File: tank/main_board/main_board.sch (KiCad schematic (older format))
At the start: 40 parts, among them J1 PowerIn, J10 Sonar2, J11 Programming Header, J12 SigOut, J13 Conn_01x01, J14 Conn_01x01, J15 Conn_01x01, J16 PowerOut, J2 Conn_01x01, J3 Conn_01x01, J4 LED, J5 Conn_01x01, J6 Spk, J7 Hall2, J8 Hall1, J9 Sonar1, Q1 2N3904, U1 LM317_TO3, U2 ATMEGA328P-PU, U3 SN754410, U4 SN754410, Y1 Crystal

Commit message: Main Board v0.2
Adjustments to main board:
- resistors were inline when they shoulda been pull-ups
- adjust crystal footprint
- IR TX needs to be on pin 3
- silkscreen should have component names
- width of motor traces increased and added ground-fill
- motor vin isn't actually connected
- motor screw terminal footprints
- fix reset line - 1 uF cap
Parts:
- removed C7: C7, Capacitors_THT:C_Disc_D4.7mm_W2.5mm_P5.00mm, symbol C_Small
- removed J1: PowerIn, JST:JST_EH_B02B-EH-A_02x2.50mm_Straight, symbol Conn_01x02
- removed J13, J14, J15, J2, J3, J5: Conn_01x01, Connectors:1pin, symbol Conn_01x01
- removed J4: LED, JST:JST_EH_B04B-EH-A_04x2.50mm_Straight, symbol Conn_01x04
- removed R5: R5, Resistors_THT:R_Axial_DIN0207_L6.3mm_D2.5mm_P7.62mm_Horizontal, symbol R
- removed R8: R8, Resistors_THT:R_Axial_DIN0207_L6.3mm_D2.5mm_P7.62mm_Horizontal, symbol R
- removed R9: R, Resistors_THT:R_Axial_DIN0207_L6.3mm_D2.5mm_P7.62mm_Horizontal, symbol R
- added C7: CP, Capacitors_THT:CP_Radial_D4.0mm_P2.00mm, symbol CP
- added J1: Conn_01x02_Male, JST:JST_EH_B02B-EH-A_02x2.50mm_Straight, symbol Conn_01x02_Male
- added J2, J3, J5: Conn_01x02, Connectors_Terminal_Blocks:TerminalBlock_4UCON_19963_02x3.5mm_Straight, symbol Conn_01x02
- added J4: Conn_01x03_Male, JST:JST_EH_B03B-EH-A_03x2.50mm_Straight, symbol Conn_01x03_Male
- J11: footprint Connectors:Wafer_Vertical17.5x5.8x7RM2.5-6 -> Pin_Headers:Pin_Header_Straight_1x06_Pitch2.54mm
- Y1: footprint Crystals:Crystal_HC52-6mm_Vertical -> Crystals:Crystal_HC49-U_Vertical
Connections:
- net labels added: IRRx, IRTx, LED0, MEnable, SCL, SPK
- net labels removed: LED2, LED3, Reset, SLC, Sonar1, Sonar2, Speaker, TurretCal, TurretEnc
- wire segments 97 -> 77
- no-connect marks 6 -> 7
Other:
- moved on the sheet: C5, C6, J10, J11, J12, J16, J6, J7, J8, J9, R10, R3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

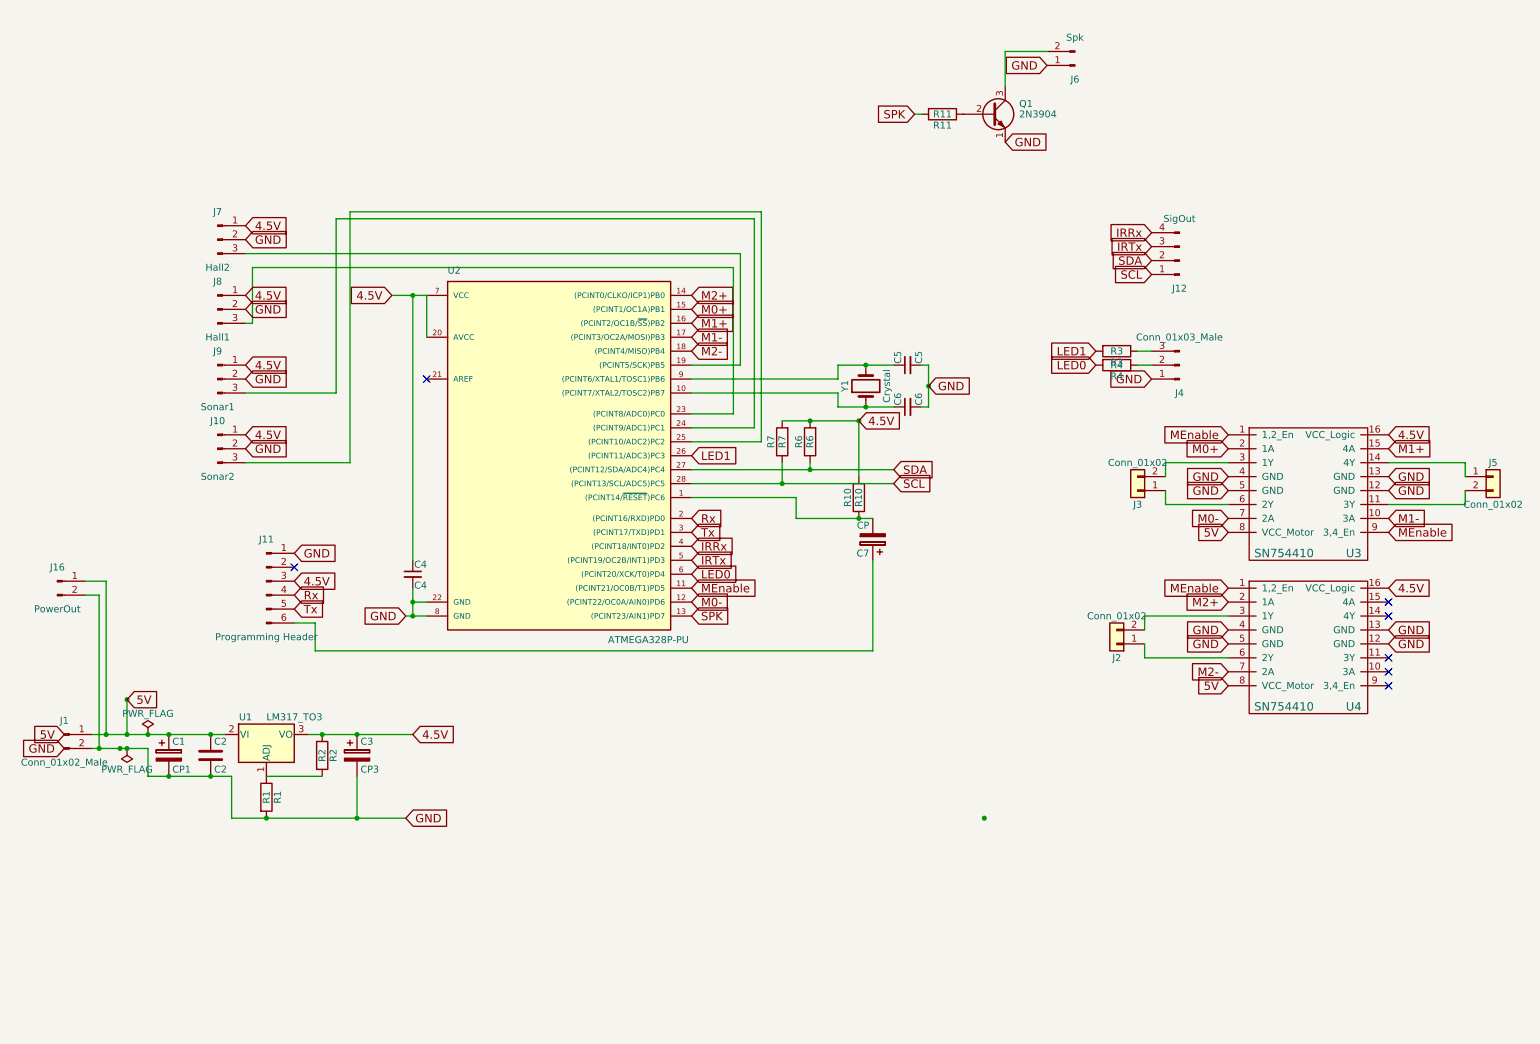
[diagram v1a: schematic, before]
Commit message: Main Board v0.3 - changed motor controllers to TB6612FNG - changed speaker transistor wiring - supports 4 LEDs, using switched ground
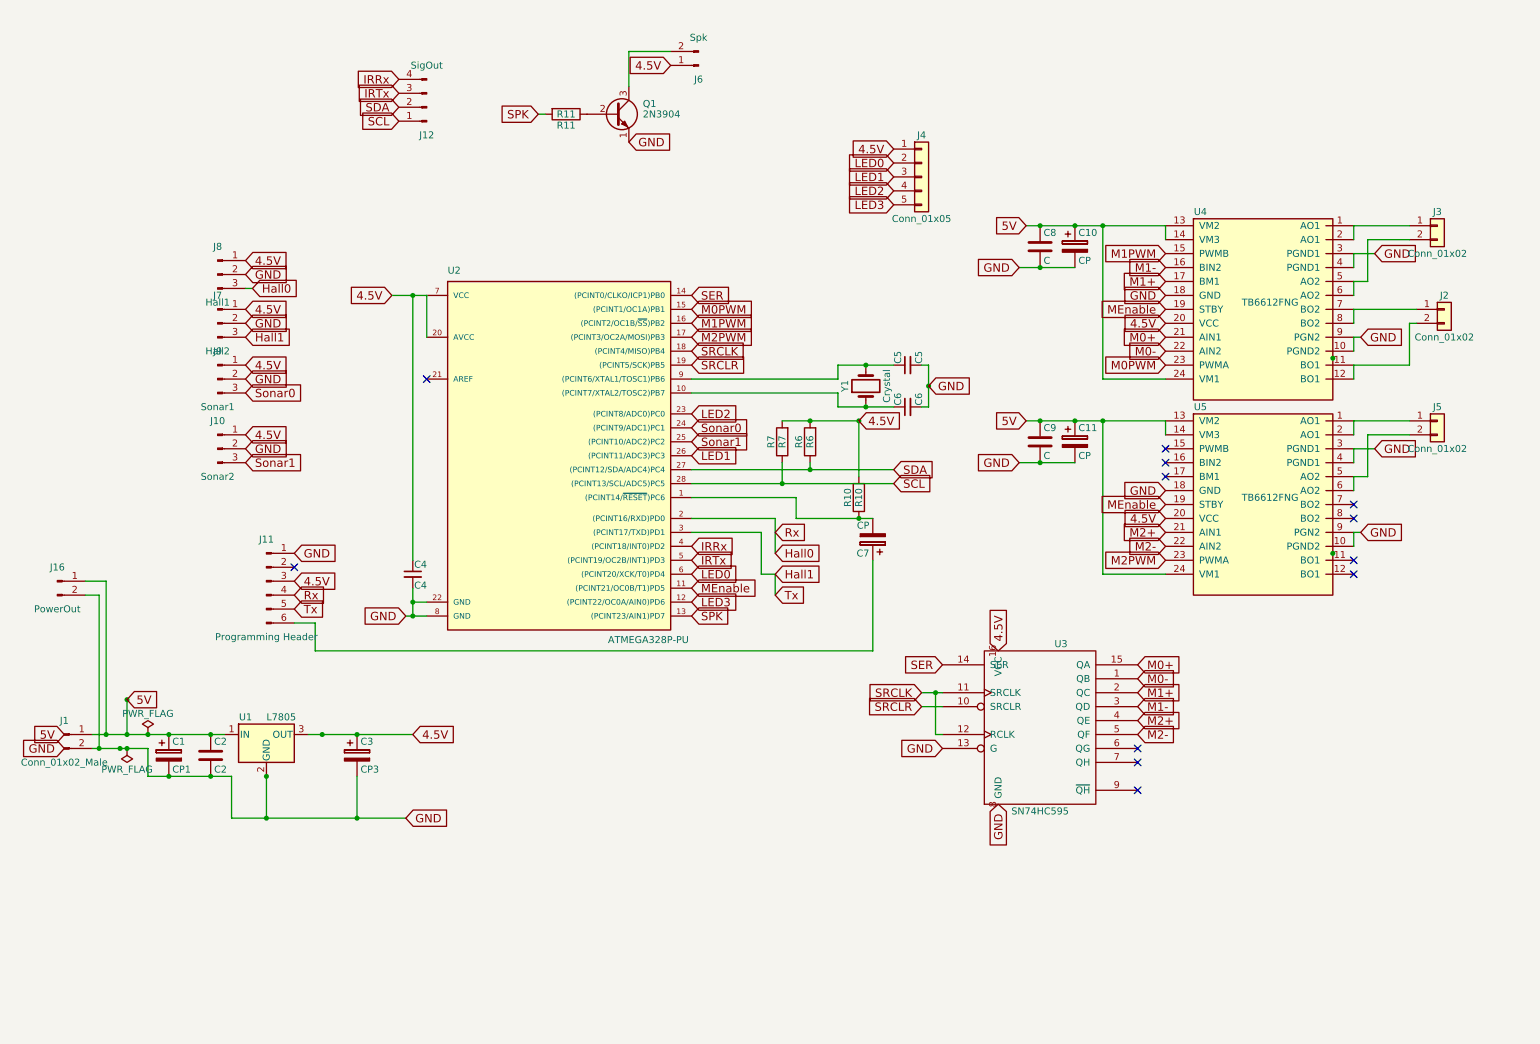
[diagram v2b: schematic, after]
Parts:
- removed J4: Conn_01x03_Male, JST:JST_EH_B03B-EH-A_03x2.50mm_Straight, symbol Conn_01x03_Male
- removed R1: R1, Resistors_THT:R_Axial_DIN0207_L6.3mm_D2.5mm_P7.62mm_Horizontal, symbol R
- removed R2: R2, Resistors_THT:R_Axial_DIN0207_L6.3mm_D2.5mm_P7.62mm_Horizontal, symbol R
- removed R3: R3, Resistors_THT:R_Axial_DIN0207_L6.3mm_D2.5mm_P7.62mm_Horizontal, symbol R
- removed R4: R4, Resistors_THT:R_Axial_DIN0207_L6.3mm_D2.5mm_P7.62mm_Horizontal, symbol R
- removed U1: LM317_TO3, Custom:LM317T, symbol LM317_TO3
- removed U3, U4: SN754410, Housings_DIP:DIP-16_W7.62mm_Socket, symbol SN754410
- added C10, C11: CP, Capacitors_THT:C_Disc_D4.7mm_W2.5mm_P5.00mm, symbol CP
- added C8: C, Capacitors_THT:C_Disc_D4.7mm_W2.5mm_P5.00mm, symbol C
- added C9: C, Capacitors_THT:CP_Radial_D4.0mm_P2.00mm, symbol C
- added J4: Conn_01x05, Connectors_JST:JST_EH_B05B-EH-A_05x2.50mm_Straight, symbol Conn_01x05
- added U1: L7805, Custom:L7805, symbol L7805
- added U3: SN74HC595, Housings_DIP:DIP-16_W7.62mm, symbol SN74HC595
- added U4, U5: TB6612FNG, Custom:TB6612FNG, symbol TB6612FNG
- J2, J3, J5: footprint Connectors_Terminal_Blocks:TerminalBlock_4UCON_19963_02x3.5mm_Straight -> Custom:TerminalBlock_4UCON_19963_02x4.5mm_Straight
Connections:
- net Rx is gone; now on net Hall0: J11.4 (Pin_4), U2.2 ((PCINT16/RXD)PD0)
- net Tx is gone; now on net Hall1: J11.5 (Pin_5), U2.3 ((PCINT17/TXD)PD1)
- net 4.5V: now also J6.1 (Pin_1), J4.1 (Pin_1), U1.3 (OUT), U3.16 (VCC), U4.20 (VCC), U5.20 (VCC)
- net 5V: now also C10.1, C11.1, C8.1, C9.1, U1.1 (IN), U4.13 (VM2), U4.14 (VM3), U4.24 (VM1), U5.13 (VM2), U5.14 (VM3), U5.24 (VM1)
- net GND: now also C10.2, C11.2, C8.2, C9.2, U1.2 (GND), U3.13 (G), U3.8 (GND), U4.10 (PGND2), U4.18 (GND), U4.3 (PGND1), U4.4 (PGND1), U4.9 (PGN2), U5.10 (PGND2), U5.18 (GND), U5.3 (PGND1), U5.4 (PGND1), U5.9 (PGN2); no longer J6.1 (Pin_1)
- net LED0: now also J4.2 (Pin_2)
- net LED1: now also J4.3 (Pin_3)
- net M0+: now also U3.15 (QA), U4.21 (AIN1); no longer U2.15 ((PCINT1/OC1A)PB1)
- net M0-: now also U3.1 (QB), U4.22 (AIN2); no longer U2.12 ((PCINT22/OC0A/AIN0)PD6)
- net M1+: now also U3.2 (QC), U4.17 (BM1); no longer U2.16 ((PCINT2/OC1B/~SS~)PB2)
- net M1-: now also U3.3 (QD), U4.16 (BIN2); no longer U2.17 ((PCINT3/OC2A/MOSI)PB3)
- net M2+: now also U3.4 (QE), U5.21 (AIN1); no longer U2.14 ((PCINT0/CLKO/ICP1)PB0)
- net M2-: now also U3.5 (QF), U5.22 (AIN2); no longer U2.18 ((PCINT4/MISO)PB4)
- net MEnable: now also U4.19 (STBY), U5.19 (STBY)
- net Hall1: now reaches J7.3 (Pin_3)
- net Hall1: no longer U2.19 ((PCINT5/SCK)PB5)
- net Hall0: now reaches J8.3 (Pin_3)
- net Hall0: no longer U2.23 ((PCINT8/ADC0)PC0)
- net Sonar0: now reaches J9.3 (Pin_3), U2.24 ((PCINT9/ADC1)PC1)
- net Sonar1: now reaches J10.3 (Pin_3), U2.25 ((PCINT10/ADC2)PC2)
- net at J5.2 (Pin_2): now also U5.5 (AO2), U5.6 (AO2)
- net at J5.1 (Pin_1): now also U5.1 (AO1), U5.2 (AO1)
- net at J3.2 (Pin_2): now also U4.5 (AO2), U4.6 (AO2)
- net at J3.1 (Pin_1): now also U4.1 (AO1), U4.2 (AO1)
- net at J2.2 (Pin_2): now also U4.11 (BO1), U4.12 (BO1)
- net at J2.1 (Pin_1): now also U4.7 (BO2), U4.8 (BO2)
- new net LED2: J4.4 (Pin_4), U2.23 ((PCINT8/ADC0)PC0)
- new net LED3: J4.5 (Pin_5), U2.12 ((PCINT22/OC0A/AIN0)PD6)
- new net M0PWM: U2.15 ((PCINT1/OC1A)PB1), U4.23 (PWMA)
- new net M1PWM: U2.16 ((PCINT2/OC1B/~SS~)PB2), U4.15 (PWMB)
- new net M2PWM: U2.17 ((PCINT3/OC2A/MOSI)PB3), U5.23 (PWMA)
- new net SER: U2.14 ((PCINT0/CLKO/ICP1)PB0), U3.14 (SER)
- new net SRCLK: U2.18 ((PCINT4/MISO)PB4), U3.11 (SRCLK), U3.12 (RCLK)
- new net SRCLR: U2.19 ((PCINT5/SCK)PB5), U3.10 (SRCLR)
- no-connect marks 7 -> 12
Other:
- moved on the sheet: J12, J2, J3, J6, J7, J8, Q1, R11

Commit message: Main Board v0.4
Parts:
- C10, C11: footprint Capacitors_THT:C_Disc_D4.7mm_W2.5mm_P5.00mm -> Capacitors_THT:CP_Radial_D4.0mm_P2.00mm
- C9: footprint Capacitors_THT:CP_Radial_D4.0mm_P2.00mm -> Capacitors_THT:C_Disc_D4.7mm_W2.5mm_P5.00mm
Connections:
- net 4.5V: no longer J4.1 (Pin_1), J6.1 (Pin_1)
- net 5V: now also J4.1 (Pin_1), J6.1 (Pin_1)
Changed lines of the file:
@@
 IRRx
 Text GLabel 5100 750  0    60   Input ~ 0
-4.5V
+5V
 $Comp
 L L7805 U1
@@
 F 0 "C10" H 8025 2150 50  0000 L CNN
 F 1 "CP" H 8025 1950 50  0000 L CNN
-F 2 "Capacitors_THT:C_Disc_D4.7mm_W2.5mm_P5.00mm" H 8038 1900 50  0001 C CNN
+F 2 "Capacitors_THT:CP_Radial_D4.0mm_P2.00mm" H 8038 1900 50  0001 C CNN
 F 3 "" H 8000 2050 50  0001 C CNN
 	1    8000 2050
@@
 $EndComp
 Text GLabel 6700 1350 0    60   Input ~ 0
-4.5V
+5V
 Text GLabel 6700 1450 0    60   Input ~ 0
 LED0
@@
 F 0 "C9" H 7775 3550 50  0000 L CNN
 F 1 "C" H 7775 3350 50  0000 L CNN
-F 2 "Capacitors_THT:CP_Radial_D4.0mm_P2.00mm" H 7788 3300 50  0001 C CNN
+F 2 "Capacitors_THT:C_Disc_D4.7mm_W2.5mm_P5.00mm" H 7788 3300 50  0001 C CNN
 F 3 "" H 7750 3450 50  0001 C CNN
 	1    7750 3450
@@
 F 0 "C11" H 8025 3550 50  0000 L CNN
 F 1 "CP" H 8025 3350 50  0000 L CNN
-F 2 "Capacitors_THT:C_Disc_D4.7mm_W2.5mm_P5.00mm" H 8038 3300 50  0001 C CNN
+F 2 "Capacitors_THT:CP_Radial_D4.0mm_P2.00mm" H 8038 3300 50  0001 C CNN
 F 3 "" H 8000 3450 50  0001 C CNN
 	1    8000 3450

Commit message: shut er down
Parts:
- J1: value Conn_01x02_Male -> PowerIn
- J2: value Conn_01x02 -> M2
- J3: value Conn_01x02 -> M1
- J4: value Conn_01x05 -> LEDs
- J5: value Conn_01x02 -> M3
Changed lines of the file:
@@
 P 10650 2500
 F 0 "J2" H 10650 2600 50  0000 C CNN
-F 1 "Conn_01x02" H 10650 2300 50  0000 C CNN
+F 1 "M2" H 10650 2300 50  0000 C CNN
 F 2 "Custom:TerminalBlock_4UCON_19963_02x4.5mm_Straight" H 10650 2500 50  0001 C CNN
 F 3 "" H 10650 2500 50  0001 C CNN
@@
 P 10600 1900
 F 0 "J3" H 10600 2000 50  0000 C CNN
-F 1 "Conn_01x02" H 10600 1700 50  0000 C CNN
+F 1 "M1" H 10600 1700 50  0000 C CNN
 F 2 "Custom:TerminalBlock_4UCON_19963_02x4.5mm_Straight" H 10600 1900 50  0001 C CNN
 F 3 "" H 10600 1900 50  0001 C CNN
@@
 P 750 5550
 F 0 "J1" H 750 5650 50  0000 C CNN
-F 1 "Conn_01x02_Male" H 750 5350 50  0000 C CNN
+F 1 "PowerIn" H 750 5350 50  0000 C CNN
 F 2 "JST:JST_EH_B02B-EH-A_02x2.50mm_Straight" H 750 5550 50  0001 C CNN
 F 3 "" H 750 5550 50  0001 C CNN
@@
 P 6900 1550
 F 0 "J4" H 6900 1850 50  0000 C CNN
-F 1 "Conn_01x05" H 6900 1250 50  0000 C CNN
+F 1 "LEDs" H 6900 1250 50  0000 C CNN
 F 2 "Connectors_JST:JST_EH_B05B-EH-A_05x2.50mm_Straight" H 6900 1550 50  0001 C CNN
 F 3 "" H 6900 1550 50  0001 C CNN
@@
 P 10600 3300
 F 0 "J5" H 10600 3400 50  0000 C CNN
-F 1 "Conn_01x02" H 10600 3100 50  0000 C CNN
+F 1 "M3" H 10600 3100 50  0000 C CNN
 F 2 "Custom:TerminalBlock_4UCON_19963_02x4.5mm_Straight" H 10600 3300 50  0001 C CNN
 F 3 "" H 10600 3300 50  0001 C CNN
@@
 $EndComp
 Connection ~ 9850 4250
-$Comp
-L TB6612FNG U5
-U 1 1 5A48BFD6
-P 9350 4150
-F 0 "U5" H 8900 5100 50  0000 C CNN
-F 1 "TB6612FNG" H 9400 4450 50  0000 C CNN
-F 2 "Custom:TB6612FNG" H 9400 3650 50  0001 C CNN
-F 3 "" H 8850 5050 50  0001 C CNN
-	1    9350 4150
-	1    0    0    -1
-$EndComp
 Wire Wire Line
 	10000 3300 10400 3300
 Wire Wire Line
-	10000 3400 10000 3300
-Wire Wire Line
 	10000 3700 10100 3700
 Wire Wire Line
@@
 Wire Wire Line
 	10100 3400 10400 3400
-Wire Wire Line
-	10000 3800 10000 3700
 Text GLabel 7650 3300 0    60   Input ~ 0
 5V
 Wire Wire Line
-	8650 3300 8650 3400
-Wire Wire Line
 	7650 3300 8650 3300
 Wire Wire Line
-	10000 3600 10000 3500
-Wire Wire Line
 	10000 3500 10150 3500
-Wire Wire Line
-	10000 4200 10000 4100
 Wire Wire Line
 	10000 4100 10050 4100
@@
 Text GLabel 7450 6050 3    60   Input ~ 0
 GND
+$Comp
+L TB6612FNG U5
+U 1 1 5A48BFD6
+P 9350 4150
+F 0 "U5" H 8900 5100 50  0000 C CNN
+F 1 "TB6612FNG" H 9400 4450 50  0000 C CNN
+F 2 "Custom:TB6612FNG" H 9400 3650 50  0001 C CNN
+F 3 "" H 8850 5050 50  0001 C CNN
+	1    9350 4150
+	1    0    0    -1
+$EndComp
+Wire Wire Line
+	10000 4200 10000 4100
+Wire Wire Line
+	10000 3800 10000 3700
+Wire Wire Line
+	10000 3600 10000 3500
+Wire Wire Line
+	10000 3400 10000 3300
+Wire Wire Line
+	8650 3300 8650 3400
 $EndSCHEMATC
